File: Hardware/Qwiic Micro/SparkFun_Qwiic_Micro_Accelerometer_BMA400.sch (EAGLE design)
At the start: 30 parts, among them J1 QWIIC_RIGHT_ANGLE, U1 BMA400

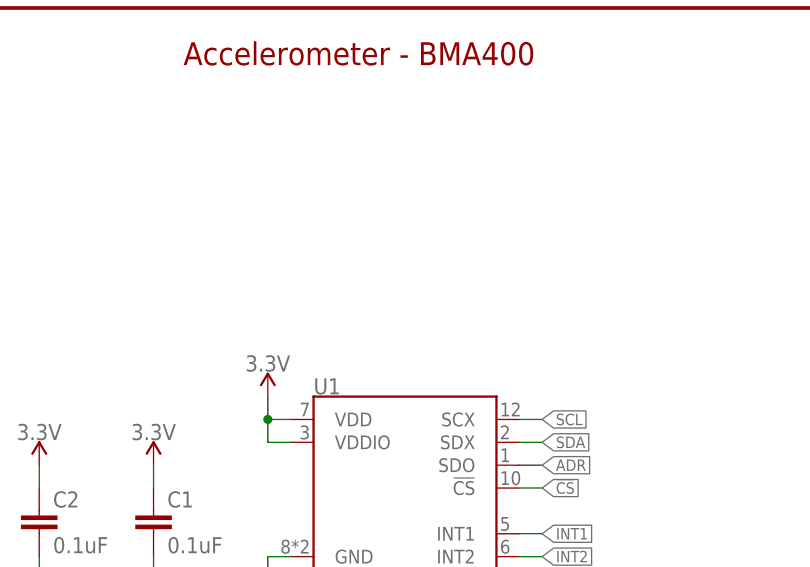
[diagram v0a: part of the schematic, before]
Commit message: Design review updates
Add BMA400 voltage range to schematics
Add designer name to boards' tDocu
Add measures to 1x1
Adjust traces of micro
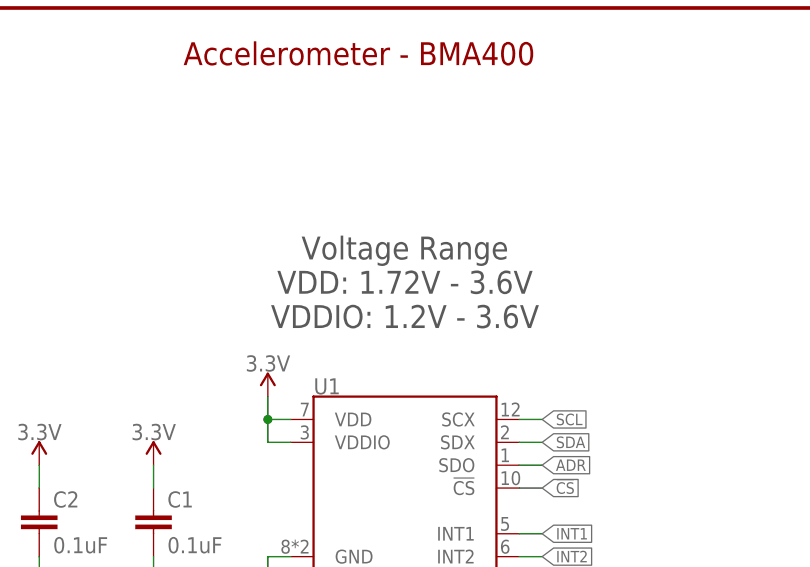
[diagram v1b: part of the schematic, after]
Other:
- note added: "Voltage Range VDD: 1.72V - 3.6V VDDIO: 1.2V - 3.6V"
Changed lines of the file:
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@@
 <text x="129.54" y="30.48" size="2.54" layer="94" font="vector" align="center">Test Points</text>
 <wire x1="147.32" y1="35.56" x2="111.76" y2="35.56" width="0.2032" layer="97" style="longdash"/>
+<text x="78.74" y="154.94" size="2.54" layer="97" font="vector" align="center">Voltage Range
+VDD: 1.72V - 3.6V
+VDDIO: 1.2V - 3.6V</text>
 </plain>
 <instances>

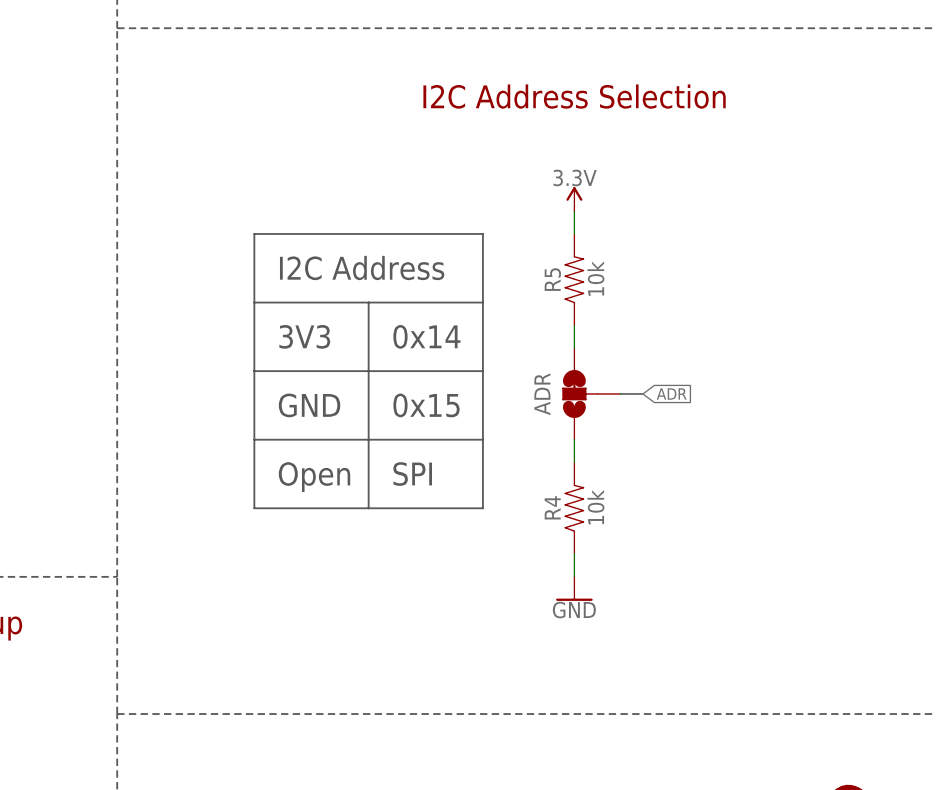
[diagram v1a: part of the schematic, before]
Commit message: Design review updates
Fix I2C address table
Add "default" to I2C address table
Approve jumper overlap errors
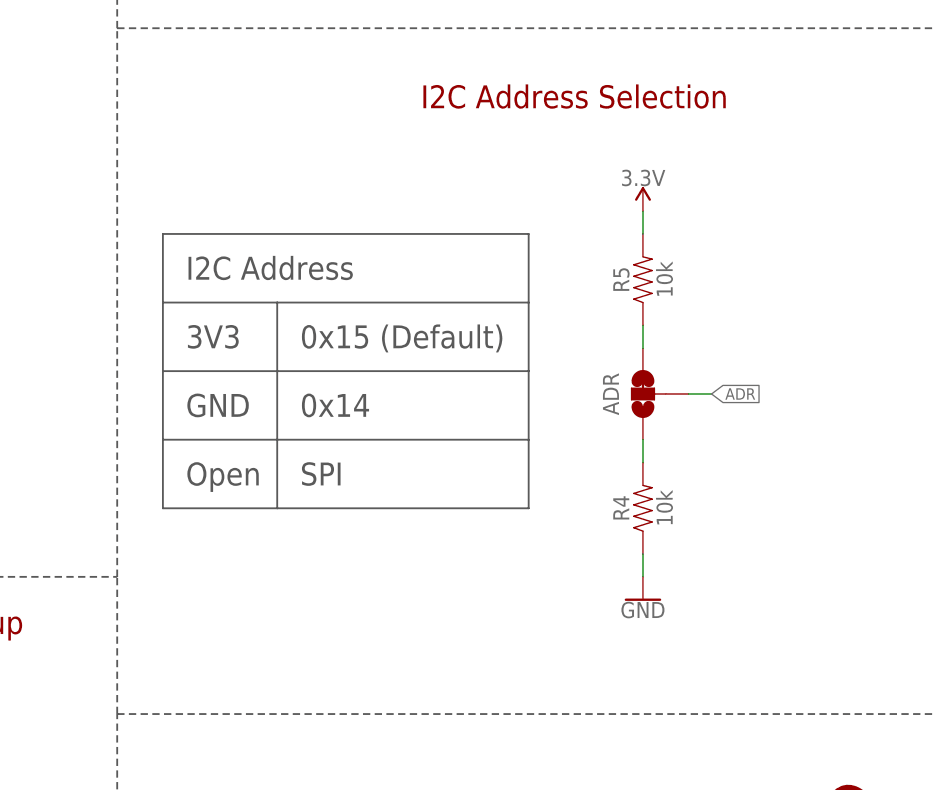
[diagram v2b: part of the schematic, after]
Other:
- note added: "0x15 (Default)"
- note removed: "0x15"
- moved on the sheet: ADR, R4, R5
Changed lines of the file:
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@@
 <wire x1="147.32" y1="66.04" x2="248.92" y2="66.04" width="0.2032" layer="97" style="longdash"/>
 <wire x1="147.32" y1="142.24" x2="248.92" y2="142.24" width="0.2032" layer="97" style="longdash"/>
-<text x="165.1" y="114.3" size="2.54" layer="97" font="vector">I2C Address</text>
-<text x="165.1" y="99.06" size="2.54" layer="97" font="vector">GND</text>
-<text x="165.1" y="106.68" size="2.54" layer="97" font="vector">3V3</text>
-<text x="165.1" y="91.44" size="2.54" layer="97" font="vector">Open</text>
-<text x="177.8" y="106.68" size="2.54" layer="97" font="vector">0x14</text>
-<text x="177.8" y="99.06" size="2.54" layer="97" font="vector">0x15</text>
-<text x="177.8" y="91.44" size="2.54" layer="97" font="vector">SPI</text>
-<wire x1="162.56" y1="119.38" x2="187.96" y2="119.38" width="0.2032" layer="97"/>
-<wire x1="187.96" y1="119.38" x2="187.96" y2="111.76" width="0.2032" layer="97"/>
-<wire x1="187.96" y1="111.76" x2="187.96" y2="104.14" width="0.2032" layer="97"/>
-<wire x1="187.96" y1="104.14" x2="187.96" y2="96.52" width="0.2032" layer="97"/>
-<wire x1="187.96" y1="96.52" x2="187.96" y2="88.9" width="0.2032" layer="97"/>
-<wire x1="187.96" y1="88.9" x2="175.26" y2="88.9" width="0.2032" layer="97"/>
-<wire x1="175.26" y1="88.9" x2="162.56" y2="88.9" width="0.2032" layer="97"/>
-<wire x1="162.56" y1="88.9" x2="162.56" y2="96.52" width="0.2032" layer="97"/>
-<wire x1="162.56" y1="96.52" x2="162.56" y2="104.14" width="0.2032" layer="97"/>
-<wire x1="162.56" y1="104.14" x2="162.56" y2="111.76" width="0.2032" layer="97"/>
-<wire x1="162.56" y1="111.76" x2="162.56" y2="119.38" width="0.2032" layer="97"/>
-<wire x1="162.56" y1="111.76" x2="175.26" y2="111.76" width="0.2032" layer="97"/>
-<wire x1="175.26" y1="111.76" x2="187.96" y2="111.76" width="0.2032" layer="97"/>
-<wire x1="162.56" y1="104.14" x2="187.96" y2="104.14" width="0.2032" layer="97"/>
-<wire x1="162.56" y1="96.52" x2="187.96" y2="96.52" width="0.2032" layer="97"/>
-<wire x1="175.26" y1="88.9" x2="175.26" y2="111.76" width="0.2032" layer="97"/>
+<text x="154.94" y="114.3" size="2.54" layer="97" font="vector">I2C Address</text>
+<text x="154.94" y="99.06" size="2.54" layer="97" font="vector">GND</text>
+<text x="154.94" y="106.68" size="2.54" layer="97" font="vector">3V3</text>
+<text x="154.94" y="91.44" size="2.54" layer="97" font="vector">Open</text>
+<text x="167.64" y="106.68" size="2.54" layer="97" font="vector">0x15 (Default)</text>
+<text x="167.64" y="99.06" size="2.54" layer="97" font="vector">0x14</text>
+<text x="167.64" y="91.44" size="2.54" layer="97" font="vector">SPI</text>
+<wire x1="152.4" y1="119.38" x2="193.04" y2="119.38" width="0.2032" layer="97"/>
+<wire x1="193.04" y1="119.38" x2="193.04" y2="111.76" width="0.2032" layer="97"/>
+<wire x1="193.04" y1="111.76" x2="193.04" y2="104.14" width="0.2032" layer="97"/>
+<wire x1="193.04" y1="104.14" x2="193.04" y2="96.52" width="0.2032" layer="97"/>
+<wire x1="193.04" y1="96.52" x2="193.04" y2="88.9" width="0.2032" layer="97"/>
+<wire x1="193.04" y1="88.9" x2="165.1" y2="88.9" width="0.2032" layer="97"/>
+<wire x1="165.1" y1="88.9" x2="152.4" y2="88.9" width="0.2032" layer="97"/>
+<wire x1="152.4" y1="88.9" x2="152.4" y2="96.52" width="0.2032" layer="97"/>
+<wire x1="152.4" y1="96.52" x2="152.4" y2="104.14" width="0.2032" layer="97"/>
+<wire x1="152.4" y1="104.14" x2="152.4" y2="111.76" width="0.2032" layer="97"/>
+<wire x1="152.4" y1="111.76" x2="152.4" y2="119.38" width="0.2032" layer="97"/>
+<wire x1="152.4" y1="111.76" x2="165.1" y2="111.76" width="0.2032" layer="97"/>
+<wire x1="165.1" y1="111.76" x2="193.04" y2="111.76" width="0.2032" layer="97"/>
+<wire x1="152.4" y1="104.14" x2="193.04" y2="104.14" width="0.2032" layer="97"/>
+<wire x1="152.4" y1="96.52" x2="193.04" y2="96.52" width="0.2032" layer="97"/>
+<wire x1="165.1" y1="88.9" x2="165.1" y2="111.76" width="0.2032" layer="97"/>
 <text x="198.12" y="149.86" size="2.54" layer="97" font="vector" align="center">Cut traces to disconnect I2C pullup resistors</text>
 <text x="93.98" y="12.7" size="2.54" layer="97" font="vector" align="center">Cut trace to
@@
 <attribute name="VALUE" x="210.82" y="158.496" size="1.778" layer="96" font="vector" align="top-center"/>
 </instance>
-<instance part="R4" gate="G$1" x="198.12" y="88.9" smashed="yes" rot="R90">
-<attribute name="NAME" x="196.596" y="88.9" size="1.778" layer="95" font="vector" rot="R90" align="bottom-center"/>
-<attribute name="VALUE" x="199.644" y="88.9" size="1.778" layer="96" font="vector" rot="R90" align="top-center"/>
-</instance>
-<instance part="R5" gate="G$1" x="198.12" y="114.3" smashed="yes" rot="R90">
-<attribute name="NAME" x="196.596" y="114.3" size="1.778" layer="95" font="vector" rot="R90" align="bottom-center"/>
-<attribute name="VALUE" x="199.644" y="114.3" size="1.778" layer="96" font="vector" rot="R90" align="top-center"/>
-</instance>
-<instance part="SUPPLY9" gate="G$1" x="198.12" y="121.92" smashed="yes">
-<attribute name="VALUE" x="198.12" y="124.714" size="1.778" layer="96" align="bottom-center"/>
-</instance>
-<instance part="GND8" gate="1" x="198.12" y="78.74" smashed="yes">
-<attribute name="VALUE" x="198.12" y="78.486" size="1.778" layer="96" align="top-center"/>
-</instance>
-<instance part="ADR" gate="G$1" x="198.12" y="101.6" smashed="yes" rot="R180">
-<attribute name="NAME" x="194.564" y="101.6" size="1.778" layer="95" font="vector" rot="R270" align="center"/>
+<instance part="R4" gate="G$1" x="205.74" y="88.9" smashed="yes" rot="R90">
+<attribute name="NAME" x="204.216" y="88.9" size="1.778" layer="95" font="vector" rot="R90" align="bottom-center"/>
+<attribute name="VALUE" x="207.264" y="88.9" size="1.778" layer="96" font="vector" rot="R90" align="top-center"/>
+</instance>
+<instance part="R5" gate="G$1" x="205.74" y="114.3" smashed="yes" rot="R90">
+<attribute name="NAME" x="204.216" y="114.3" size="1.778" layer="95" font="vector" rot="R90" align="bottom-center"/>
+<attribute name="VALUE" x="207.264" y="114.3" size="1.778" layer="96" font="vector" rot="R90" align="top-center"/>
+</instance>
+<instance part="SUPPLY9" gate="G$1" x="205.74" y="121.92" smashed="yes">
+<attribute name="VALUE" x="205.74" y="124.714" size="1.778" layer="96" align="bottom-center"/>
+</instance>
+<instance part="GND8" gate="1" x="205.74" y="78.74" smashed="yes">
+<attribute name="VALUE" x="205.74" y="78.486" size="1.778" layer="96" align="top-center"/>
+</instance>
+<instance part="ADR" gate="G$1" x="205.74" y="101.6" smashed="yes" rot="R180">
+<attribute name="NAME" x="202.184" y="101.6" size="1.778" layer="95" font="vector" rot="R270" align="center"/>
 </instance>
 <instance part="R6" gate="G$1" x="129.54" y="55.88" smashed="yes" rot="R90">
@@
 <segment>
 <pinref part="GND8" gate="1" pin="GND"/>
-<wire x1="198.12" y1="81.28" x2="198.12" y2="83.82" width="0.1524" layer="91"/>
+<wire x1="205.74" y1="81.28" x2="205.74" y2="83.82" width="0.1524" layer="91"/>
 <pinref part="R4" gate="G$1" pin="1"/>
 </segment>
@@
 </segment>
 <segment>
-<wire x1="198.12" y1="119.38" x2="198.12" y2="121.92" width="0.1524" layer="91"/>
+<wire x1="205.74" y1="119.38" x2="205.74" y2="121.92" width="0.1524" layer="91"/>
 <pinref part="SUPPLY9" gate="G$1" pin="3.3V"/>
 <pinref part="R5" gate="G$1" pin="2"/>
@@
 <segment>
 <pinref part="ADR" gate="G$1" pin="2"/>
-<wire x1="203.2" y1="101.6" x2="205.74" y2="101.6" width="0.1524" layer="91"/>
-<label x="205.74" y="101.6" size="1.27" layer="95" font="vector" xref="yes"/>
+<wire x1="210.82" y1="101.6" x2="213.36" y2="101.6" width="0.1524" layer="91"/>
+<label x="213.36" y="101.6" size="1.27" layer="95" font="vector" xref="yes"/>
 </segment>
 </net>
@@
 <segment>
 <pinref part="R5" gate="G$1" pin="1"/>
-<wire x1="198.12" y1="109.22" x2="198.12" y2="106.68" width="0.1524" layer="91"/>
+<wire x1="205.74" y1="109.22" x2="205.74" y2="106.68" width="0.1524" layer="91"/>
 <pinref part="ADR" gate="G$1" pin="3"/>
 </segment>
@@
 <segment>
 <pinref part="R4" gate="G$1" pin="2"/>
-<wire x1="198.12" y1="93.98" x2="198.12" y2="96.52" width="0.1524" layer="91"/>
+<wire x1="205.74" y1="93.98" x2="205.74" y2="96.52" width="0.1524" layer="91"/>
 <pinref part="ADR" gate="G$1" pin="1"/>
 </segment>

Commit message: Change default I2C address
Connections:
- net N$5: now also ADR.1; no longer ADR.3
- net N$6: now also ADR.3; no longer ADR.1
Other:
- note added: "0x14 (Default)"
- note added: "0x15"
- note removed: "0x14"
- note removed: "0x15 (Default)"
- moved on the sheet: ADR
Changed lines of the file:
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@@
 <part name="SUPPLY9" library="SparkFun-PowerSymbols" deviceset="3.3V" device=""/>
 <part name="GND8" library="SparkFun-PowerSymbols" deviceset="GND" device=""/>
-<part name="ADR" library="SparkFun-Jumpers" deviceset="JUMPER-SMT_3_1-NC_TRACE" device="_SILK" package3d_urn="urn:adsk.eagle:package:39288/1"/>
 <part name="R6" library="SparkFun-Resistors" deviceset="10KOHM" device="-0402T-1/16W-1%" value="10k"/>
 <part name="SUPPLY10" library="SparkFun-PowerSymbols" deviceset="3.3V" device=""/>
@@
 <part name="LOGO4" library="SparkFun-Aesthetics" deviceset="SFE_LOGO_FLAME" device=".1_INCH"/>
 <part name="GND2" library="SparkFun-PowerSymbols" deviceset="GND" device=""/>
+<part name="ADR" library="SparkFun-Jumpers" deviceset="JUMPER-SMT_3_1-NC_TRACE" device="_SILK" package3d_urn="urn:adsk.eagle:package:39288/1"/>
 </parts>
 <sheets>
@@
 <text x="154.94" y="106.68" size="2.54" layer="97" font="vector">3V3</text>
 <text x="154.94" y="91.44" size="2.54" layer="97" font="vector">Open</text>
-<text x="167.64" y="106.68" size="2.54" layer="97" font="vector">0x15 (Default)</text>
-<text x="167.64" y="99.06" size="2.54" layer="97" font="vector">0x14</text>
+<text x="167.64" y="106.68" size="2.54" layer="97" font="vector">0x15</text>
+<text x="167.64" y="99.06" size="2.54" layer="97" font="vector">0x14 (Default)</text>
 <text x="167.64" y="91.44" size="2.54" layer="97" font="vector">SPI</text>
 <wire x1="152.4" y1="119.38" x2="193.04" y2="119.38" width="0.2032" layer="97"/>
@@
 <attribute name="VALUE" x="205.74" y="78.486" size="1.778" layer="96" align="top-center"/>
 </instance>
-<instance part="ADR" gate="G$1" x="205.74" y="101.6" smashed="yes" rot="R180">
-<attribute name="NAME" x="202.184" y="101.6" size="1.778" layer="95" font="vector" rot="R270" align="center"/>
-</instance>
 <instance part="R6" gate="G$1" x="129.54" y="55.88" smashed="yes" rot="R90">
 <attribute name="NAME" x="128.016" y="55.88" size="1.778" layer="95" font="vector" rot="R90" align="bottom-center"/>
@@
 <instance part="GND2" gate="1" x="43.18" y="45.72" smashed="yes">
 <attribute name="VALUE" x="43.18" y="45.466" size="1.778" layer="96" align="top-center"/>
+</instance>
+<instance part="ADR" gate="G$1" x="205.74" y="101.6" smashed="yes" rot="MR0">
+<attribute name="NAME" x="202.184" y="101.6" size="1.778" layer="95" font="vector" rot="MR90" align="center"/>
 </instance>
 </instances>
@@
 </segment>
 <segment>
-<pinref part="ADR" gate="G$1" pin="2"/>
 <wire x1="210.82" y1="101.6" x2="213.36" y2="101.6" width="0.1524" layer="91"/>
 <label x="213.36" y="101.6" size="1.27" layer="95" font="vector" xref="yes"/>
+<pinref part="ADR" gate="G$1" pin="2"/>
 </segment>
 </net>
@@
 <pinref part="R5" gate="G$1" pin="1"/>
 <wire x1="205.74" y1="109.22" x2="205.74" y2="106.68" width="0.1524" layer="91"/>
-<pinref part="ADR" gate="G$1" pin="3"/>
+<pinref part="ADR" gate="G$1" pin="1"/>
 </segment>
 </net>
@@
 <pinref part="R4" gate="G$1" pin="2"/>
 <wire x1="205.74" y1="93.98" x2="205.74" y2="96.52" width="0.1524" layer="91"/>
-<pinref part="ADR" gate="G$1" pin="1"/>
-</segment>
-</net>
+<pinref part="ADR" gate="G$1" pin="3"/>
+</segment>
+</net>
